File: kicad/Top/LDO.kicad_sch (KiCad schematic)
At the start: 14 parts, among them U2 TLV76033DBZR

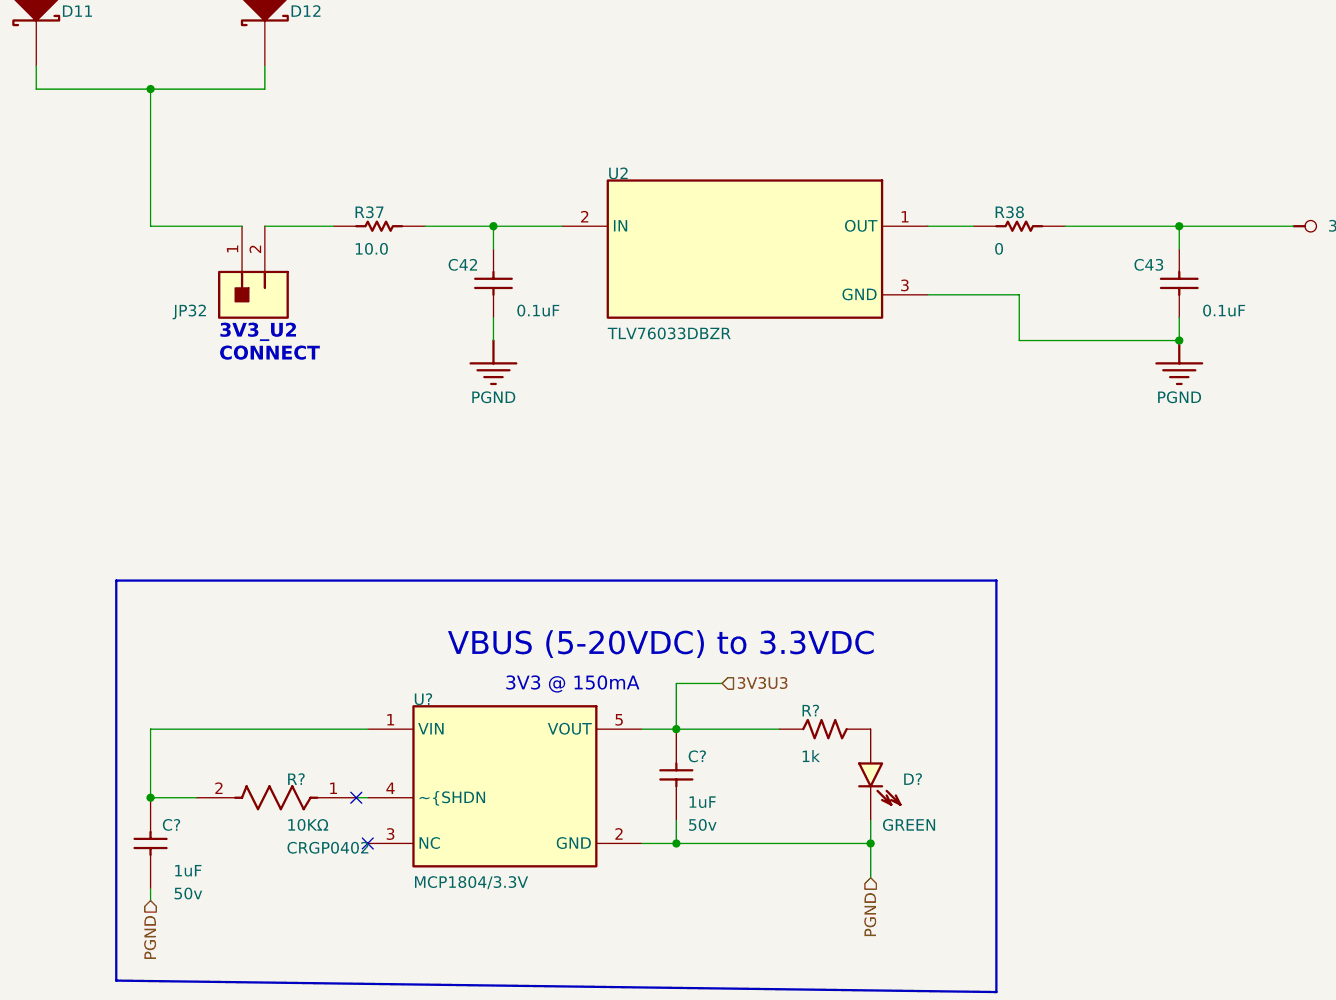
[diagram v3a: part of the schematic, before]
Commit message: Added minimal RP mcu sheet
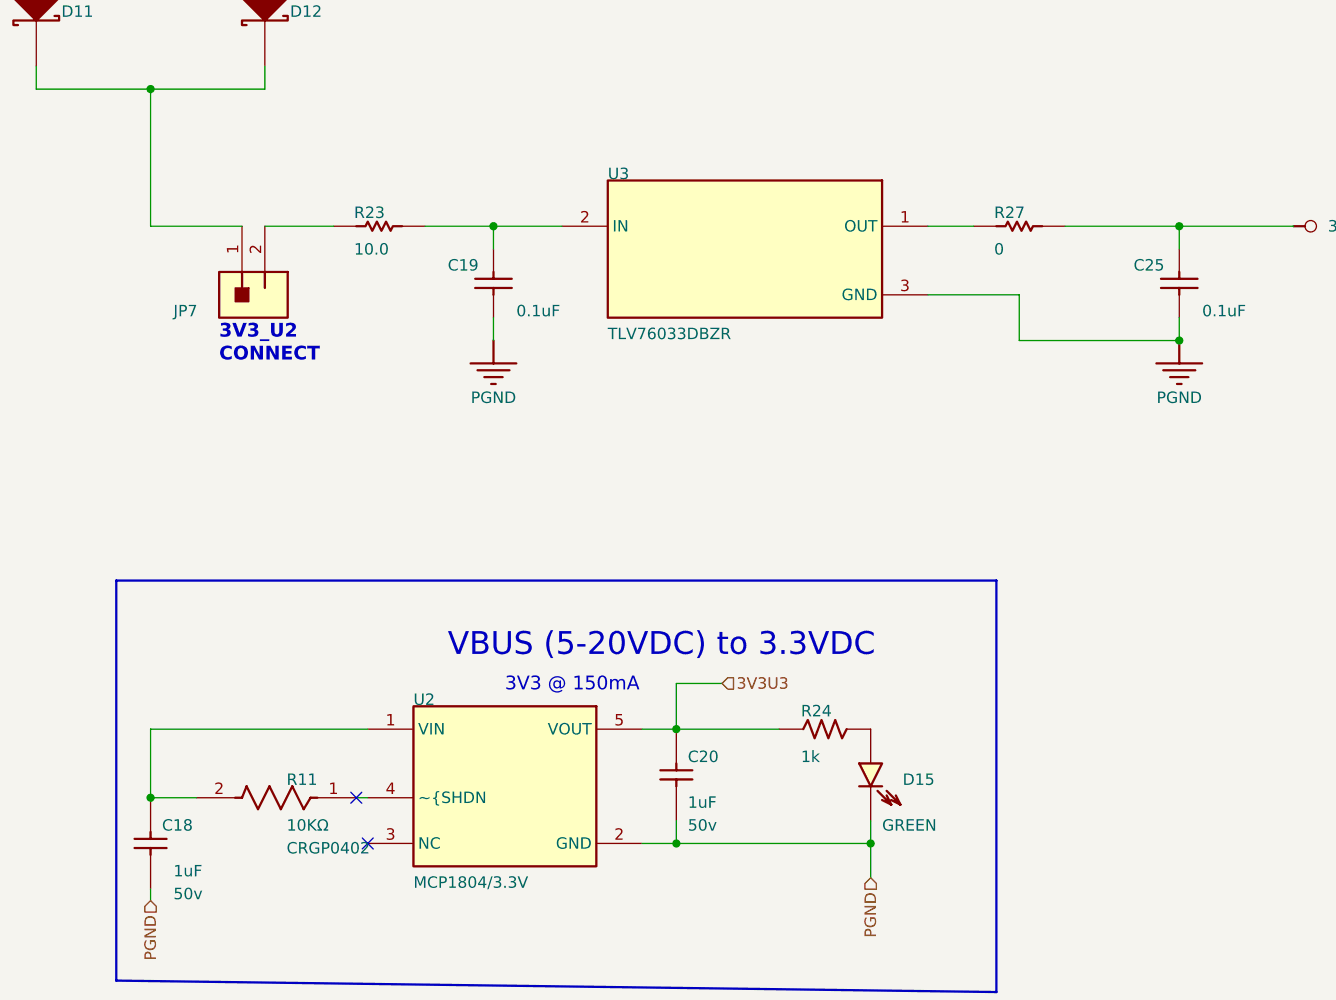
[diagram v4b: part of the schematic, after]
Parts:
- gave numbers to parts that had none: 6
- renumbered C42 to C19, C43 to C25, JP32 to JP7, R37 to R23, R38 to R27, U2 to U3
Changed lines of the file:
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@@
   (symbol (lib_id "Top-altium-import:0_CMP-0020833-2") (at 157.48 116.84 0) (unit 1)
     (in_bom yes) (on_board yes)
-    (property "Reference" "R38" (id 0) (at 154.686 116.078 0)
+    (property "Reference" "R27" (id 0) (at 154.686 116.078 0)
       (effects (font (size 1.27 1.27)) (justify left bottom))
     )
@@
   (symbol (lib_id "Top-altium-import:3V3_U2") (at 124.46 68.58 90) (unit 1)
     (in_bom yes) (on_board yes)
-    (property "Reference" "#PWR0253" (id 0) (at 124.46 68.58 0)
+    (property "Reference" "#PWR0102" (id 0) (at 124.46 68.58 0)
       (effects (font (size 1.27 1.27)) hide)
     )
@@
   (symbol (lib_id "Top-altium-import:3_mirrored_CMP-0002337-1") (at 71.12 121.92 0) (unit 1)
     (in_bom yes) (on_board yes)
-    (property "Reference" "JP32" (id 0) (at 63.5 127 0)
+    (property "Reference" "JP7" (id 0) (at 63.5 127 0)
       (effects (font (size 1.27 1.27)) (justify left bottom))
     )
@@
   (symbol (lib_id "Top-altium-import:BAT_U1") (at 71.12 81.28 270) (unit 1)
     (in_bom yes) (on_board yes)
-    (property "Reference" "#PWR0255" (id 0) (at 71.12 81.28 0)
+    (property "Reference" "#PWR0104" (id 0) (at 71.12 81.28 0)
       (effects (font (size 1.27 1.27)) hide)
     )
@@
   (symbol (lib_id "Top-altium-import:3_LED_green") (at 140.97 172.72 0) (unit 1)
     (in_bom yes) (on_board yes)
-    (property "Reference" "D?" (id 0) (at 144.526 179.07 0)
+    (property "Reference" "D15" (id 0) (at 144.526 179.07 0)
       (effects (font (size 1.27 1.27)) (justify left bottom))
     )
@@
   (symbol (lib_id "Top-altium-import:PGND") (at 64.77 58.42 0) (unit 1)
     (in_bom yes) (on_board yes)
-    (property "Reference" "#PWR0256" (id 0) (at 64.77 58.42 0)
+    (property "Reference" "#PWR0105" (id 0) (at 64.77 58.42 0)
       (effects (font (size 1.27 1.27)) hide)
     )
@@
   (symbol (lib_id "Top-altium-import:PGND") (at 175.26 129.54 0) (unit 1)
     (in_bom yes) (on_board yes)
-    (property "Reference" "#PWR0258" (id 0) (at 175.26 129.54 0)
+    (property "Reference" "#PWR0108" (id 0) (at 175.26 129.54 0)
       (effects (font (size 1.27 1.27)) hide)
     )
@@
   (symbol (lib_id "Top-altium-import:PGND") (at 99.06 129.54 0) (unit 1)
     (in_bom yes) (on_board yes)
-    (property "Reference" "#PWR0260" (id 0) (at 99.06 129.54 0)
+    (property "Reference" "#PWR0107" (id 0) (at 99.06 129.54 0)
       (effects (font (size 1.27 1.27)) hide)
     )
@@
   (symbol (lib_id "Top-altium-import:VBUS") (at 45.72 81.28 270) (unit 1)
     (in_bom yes) (on_board yes)
-    (property "Reference" "#PWR0257" (id 0) (at 45.72 81.28 0)
+    (property "Reference" "#PWR0106" (id 0) (at 45.72 81.28 0)
       (effects (font (size 1.27 1.27)) hide)
     )
@@
   (symbol (lib_id "Top-altium-import:BAT_U1") (at 124.46 53.34 90) (unit 1)
     (in_bom yes) (on_board yes)
-    (property "Reference" "#PWR0252" (id 0) (at 124.46 53.34 0)
+    (property "Reference" "#PWR0101" (id 0) (at 124.46 53.34 0)
       (effects (font (size 1.27 1.27)) hide)
     )
@@
   (symbol (lib_id "Top-altium-import:0_CMP-0074893-1") (at 127 119.38 0) (unit 1)
     (in_bom yes) (on_board yes)
-    (property "Reference" "U2" (id 0) (at 111.76 111.76 0)
+    (property "Reference" "U3" (id 0) (at 111.76 111.76 0)
       (effects (font (size 1.27 1.27)) (justify left bottom))
     )
@@
   (symbol (lib_id "Top-altium-import:3V3_U2") (at 187.96 116.84 90) (unit 1)
     (in_bom yes) (on_board yes)
-    (property "Reference" "#PWR0259" (id 0) (at 187.96 116.84 0)
+    (property "Reference" "#PWR0109" (id 0) (at 187.96 116.84 0)
       (effects (font (size 1.27 1.27)) hide)
     )
@@
   (symbol (lib_id "Top-altium-import:3_CMP-0006607-2") (at 175.26 121.92 0) (unit 1)
     (in_bom yes) (on_board yes)
-    (property "Reference" "C43" (id 0) (at 170.18 121.92 0)
+    (property "Reference" "C25" (id 0) (at 170.18 121.92 0)
       (effects (font (size 1.27 1.27)) (justify left bottom))
     )
@@
   (symbol (lib_id "Top-altium-import:2_CMP-03211-008310-1") (at 83.82 180.34 0) (unit 1)
     (in_bom yes) (on_board yes)
-    (property "Reference" "R?" (id 0) (at 76.073 179.07 0)
+    (property "Reference" "R11" (id 0) (at 76.073 179.07 0)
       (effects (font (size 1.27 1.27)) (justify left bottom))
     )
@@
   (symbol (lib_id "Top-altium-import:0_MCP1804 SOT-23-5") (at 90.17 170.18 0) (unit 1)
     (in_bom yes) (on_board yes)
-    (property "Reference" "U?" (id 0) (at 90.17 170.18 0)
+    (property "Reference" "U2" (id 0) (at 90.17 170.18 0)
       (effects (font (size 1.27 1.27)) (justify left bottom))
     )
@@
   (symbol (lib_id "Top-altium-import:2_Resistor") (at 140.97 172.72 0) (unit 1)
     (in_bom yes) (on_board yes)
-    (property "Reference" "R?" (id 0) (at 133.223 171.45 0)
+    (property "Reference" "R24" (id 0) (at 133.223 171.45 0)
       (effects (font (size 1.27 1.27)) (justify left bottom))
     )
@@
   (symbol (lib_id "Top-altium-import:0_CMP-0017299-3") (at 86.36 116.84 0) (unit 1)
     (in_bom yes) (on_board yes)
-    (property "Reference" "R37" (id 0) (at 83.566 116.078 0)
+    (property "Reference" "R23" (id 0) (at 83.566 116.078 0)
       (effects (font (size 1.27 1.27)) (justify left bottom))
     )
@@
   (symbol (lib_id "Top-altium-import:1_Capacitor NP") (at 119.38 182.88 0) (unit 1)
     (in_bom yes) (on_board yes)
-    (property "Reference" "C?" (id 0) (at 120.65 176.53 0)
+    (property "Reference" "C20" (id 0) (at 120.65 176.53 0)
       (effects (font (size 1.27 1.27)) (justify left bottom))
     )
@@
   (symbol (lib_id "Top-altium-import:1_Capacitor NP") (at 60.96 190.5 0) (unit 1)
     (in_bom yes) (on_board yes)
-    (property "Reference" "C?" (id 0) (at 62.23 184.15 0)
+    (property "Reference" "C18" (id 0) (at 62.23 184.15 0)
       (effects (font (size 1.27 1.27)) (justify left bottom))
     )
@@
   (symbol (lib_id "Top-altium-import:3_CMP-0006607-2") (at 99.06 121.92 0) (unit 1)
     (in_bom yes) (on_board yes)
-    (property "Reference" "C42" (id 0) (at 93.98 121.92 0)
+    (property "Reference" "C19" (id 0) (at 93.98 121.92 0)
       (effects (font (size 1.27 1.27)) (justify left bottom))
     )
@@
   (symbol (lib_id "Top-altium-import:VBUS") (at 124.46 60.96 90) (unit 1)
     (in_bom yes) (on_board yes)
-    (property "Reference" "#PWR0254" (id 0) (at 124.46 60.96 0)
-      (effects (font (size 1.27 1.27)) hide)
-    )
+    (property "Reference" "#PWR0103" (id 0) (at 124.46 60.96 0)
+      (effects (font (size 1.27 1.27)) hide)
+    )

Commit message: wip
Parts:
- removed C18, C20: Capacitor NP, AltiumImports:_ALTIUM_WORK_00001_MCHP-CDB_Library_Database_.._Footprints_CAP_C_0603.PcbLib_CAP_C_0603, symbol Top-altium-import:1_Capacitor NP
- removed C19, C25: GRM155R61E104KA87D, AltiumImports:0402L, symbol Top-altium-import:3_CMP-0006607-2
- removed D11, D12: BAT54HT1G, AltiumImports:SOD-323, symbol Top-altium-import:1_CMP-0028455-2
- removed D15: LED_green, AltiumImports:_ALTIUM_WORK_00001_MCHP-CDB_Library_Database_.._Footprints_LED_0603_Green.PcbLib_LED_0603_GREEN, symbol Top-altium-import:3_LED_green
- removed JP7: Header_2x1, AltiumImports:CONN_PEC02SAAN, symbol Top-altium-import:3_mirrored_CMP-0002337-1
- removed R11: CRGP0402F10K, AltiumImports:FP-CRGP0402-IPC_A, symbol Top-altium-import:2_CMP-03211-008310-1
- removed R23: ERJ-8ENF10R0V, AltiumImports:1206, symbol Top-altium-import:0_CMP-0017299-3
- removed R24: Resistor, AltiumImports:_ALTIUM_WORK_00001_MCHP-CDB_Library_Database_MCHP-CDB.DbLib_Resistor_RES_C_0402, symbol Top-altium-import:2_Resistor
- removed R27: 5106, AltiumImports:5106, symbol Top-altium-import:0_CMP-0020833-2
- removed U2: MCP1804 SOT-23-5, AltiumImports:_ALTIUM_WORK_00001_MCHP-CDB_Library_Database_MCHP-CDB.DbLib_MCHP-Analog_SOT-23-5, symbol Top-altium-import:0_MCP1804 SOT-23-5
- removed U3: TLV76033DBZR, AltiumImports:DBZ0003A_N, symbol Top-altium-import:0_CMP-0074893-1
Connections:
- no-connect marks 2 -> 0
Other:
- note added: "MAX77958 VBus Supply Current @ 4.2V = 150 uA MAX77976 SCL/SDA Logic Input Current = 10 uA"
- note removed: "3V3 @ 150mA"
- note removed: "3V3_U2"
- note removed: "CONNECT"
- note removed: "HARNESS: Power_Charger"
- note removed: "HARNESS: Power_External"
- note removed: "VBUS (5-20VDC) to 3.3VDC"

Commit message: wip
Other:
- note removed: "MAX77958 VBus Supply Current @ 4.2V = 150 uA MAX77976 SCL/SDA Logic Input Current = 10 uA"
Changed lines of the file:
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@@
 (kicad_sch (version 20211123) (generator eeschema)
   (paper "A")
-  (text "MAX77958 VBus Supply Current @ 4.2V = 150 uA\nMAX77976 SCL/SDA Logic Input Current = 10 uA"
-    (at 11.43 12.7 0)
-    (effects (font (size 1.27 1.27)) (justify left bottom))
+  (hierarchical_label "5V" (shape input) (at 132.08 104.14 0)
+    (effects (font (size 1.27 1.27)) (justify left))
   )
-  (hierarchical_label "VBUS" (shape input) (at 87.63 73.66 180)
+  (hierarchical_label "1V8" (shape input) (at 132.08 93.98 0)
+    (effects (font (size 1.27 1.27)) (justify left))
+  )
+  (hierarchical_label "3V3" (shape input) (at 132.08 99.06 0)
+    (effects (font (size 1.27 1.27)) (justify left))
+  )
+  (hierarchical_label "SYS" (shape input) (at 81.28 96.52 180)
     (effects (font (size 1.27 1.27)) (justify right))
   )
-  (hierarchical_label "3V3" (shape input) (at 175.26 73.66 0)
-    (effects (font (size 1.27 1.27)) (justify left))
-  )
   (sheet_instances
